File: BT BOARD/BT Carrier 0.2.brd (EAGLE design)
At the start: 16.5 x 45 mm, 3 parts, among them M1 RN4020

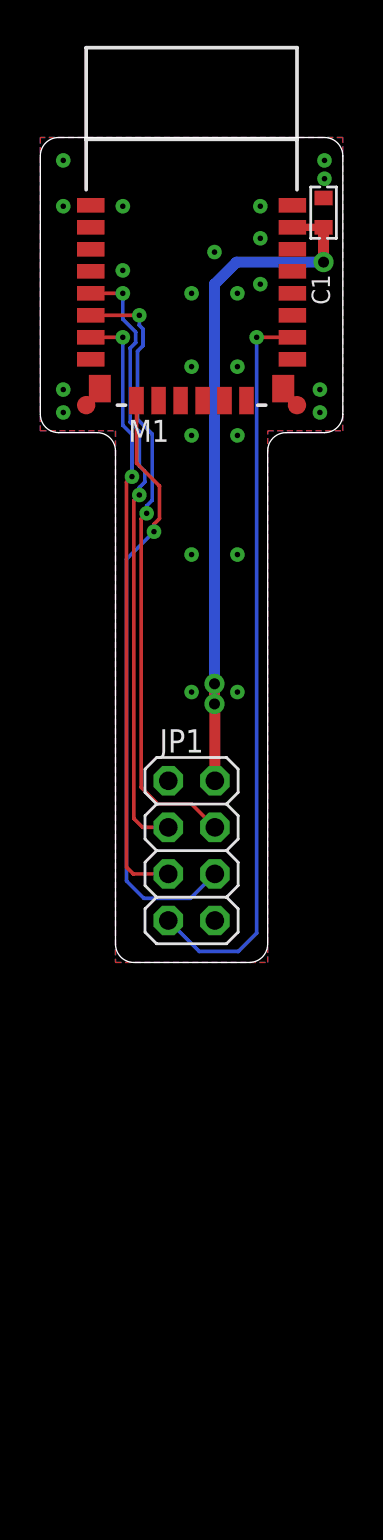
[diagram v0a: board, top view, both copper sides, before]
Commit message: added connector board
added connector board and routed. found allignment issue in BT board, and fixed it, need to get files approved by Petr and Jaroslav.
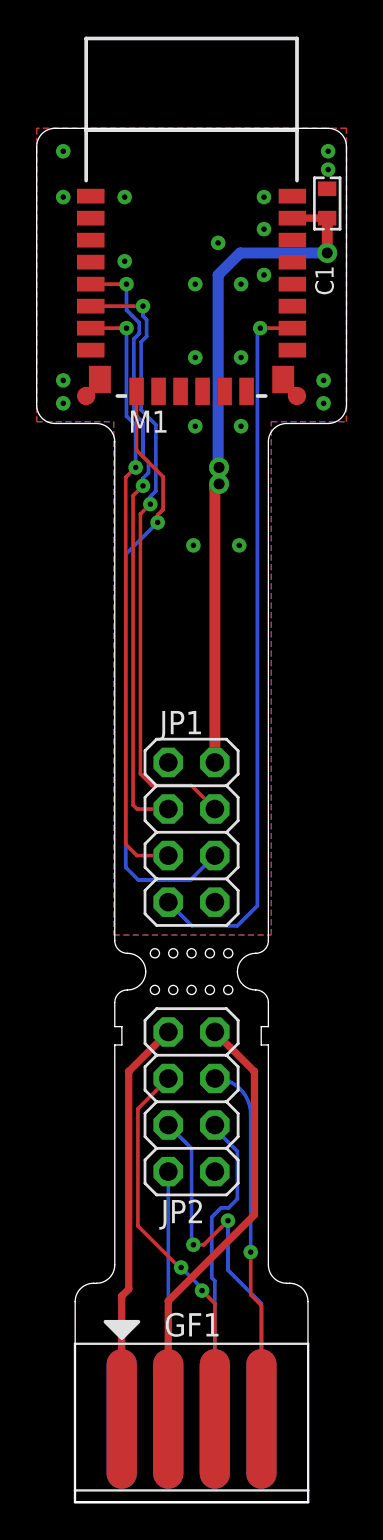
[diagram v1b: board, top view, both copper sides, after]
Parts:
- added GF1: 2X4_GOLD_FINGER, clackboard_lib:2X4_GOLD_FINGER
- added JP2: (no value), pinhead:2X04
- C1: device DISCRETE:0603 -> discrete:0603
- moved JP1 1.00 mm to (0.00, 7.10)
- moved C1 0.54 mm to (7.40, 41.4)
- moved M1 0.50 mm to (-5.75, 30.9)
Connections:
- new net +3.3V-1: GF1.3, JP2.2
- new net BT_RTS-1: GF1.4, JP2.7
- new net BT_U5RX-1: GF1.5, JP2.3
- new net BT_U5TX-1: GF1.7, JP2.4
- new net CON_LED-1: GF1.6, JP2.6
- new net DGND-1: GF1.1, JP2.1
- new net WAKE_SW-1: GF1.8, JP2.5
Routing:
- net +3.3V-1: track 0.00 -> 23.9 mm
- net DGND-1: track 0.00 -> 22.2 mm
- net WAKE_SW-1: track 0.00 -> 21.1 mm, vias 0 -> 2
- net BT_U5RX-1: track 0.00 -> 21.0 mm, vias 0 -> 2
- net BT_U5TX-1: track 0.00 -> 19.6 mm, vias 0 -> 1
- net CON_LED-1: track 0.00 -> 17.4 mm
- net BT_RTS-1: track 0.00 -> 13.5 mm
- net BT_RTS: track 40.4 -> 39.2 mm
- net +3.3V: track 38.3 -> 37.8 mm
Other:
- board size 16.5 x 45 mm -> 16.9 x 75 mm
